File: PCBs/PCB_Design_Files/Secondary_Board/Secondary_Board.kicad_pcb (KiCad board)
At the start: 4 copper layers, 40.3 x 57.1 mm, 46 parts, among them IC1 TLV2333IDGKR, IC2 320S14-U, J1 Conn_FFC_8pin, J2 Conn_01x08_Pin, Q3 MMBT3904, Q4 MMBT3904, Q5 2N7002, Q6 BSS84, Q7 2N7002, Q8 BSS84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

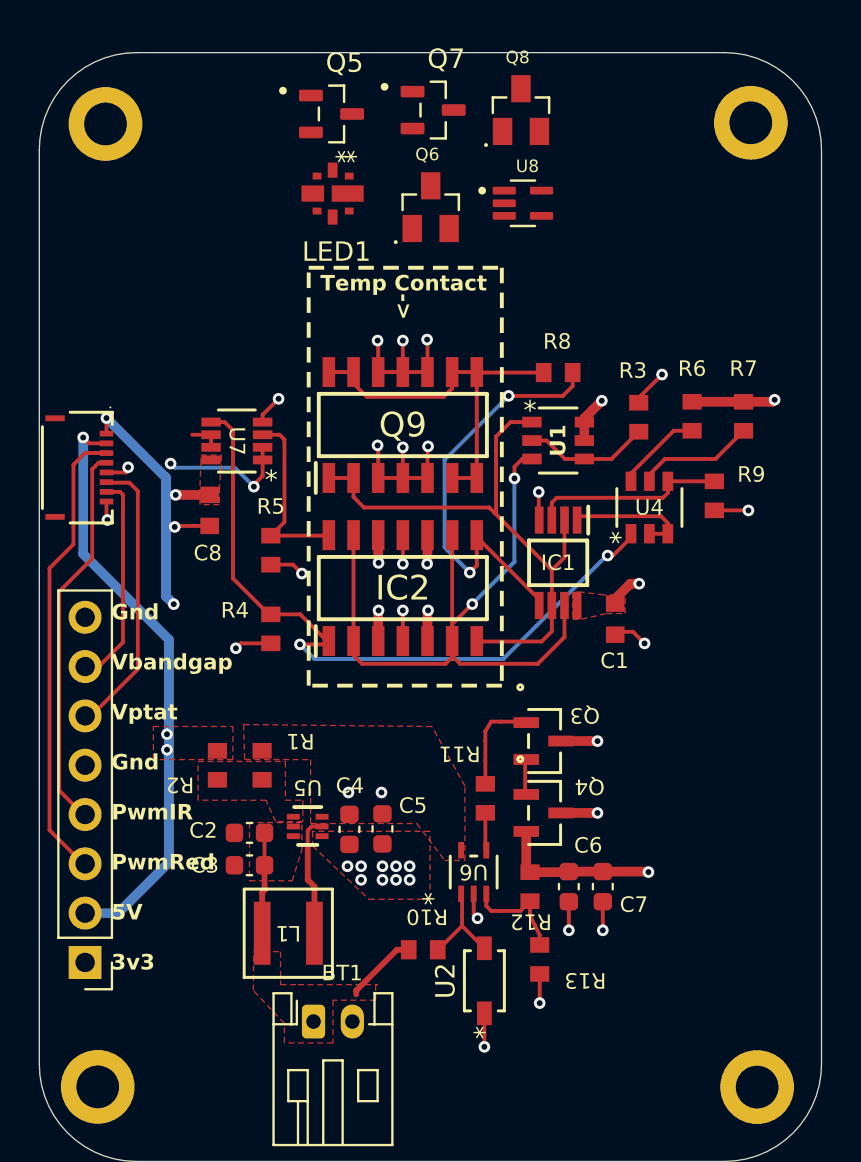
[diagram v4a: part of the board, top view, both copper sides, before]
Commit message: cleaned up ptat laout, 3v3 layer
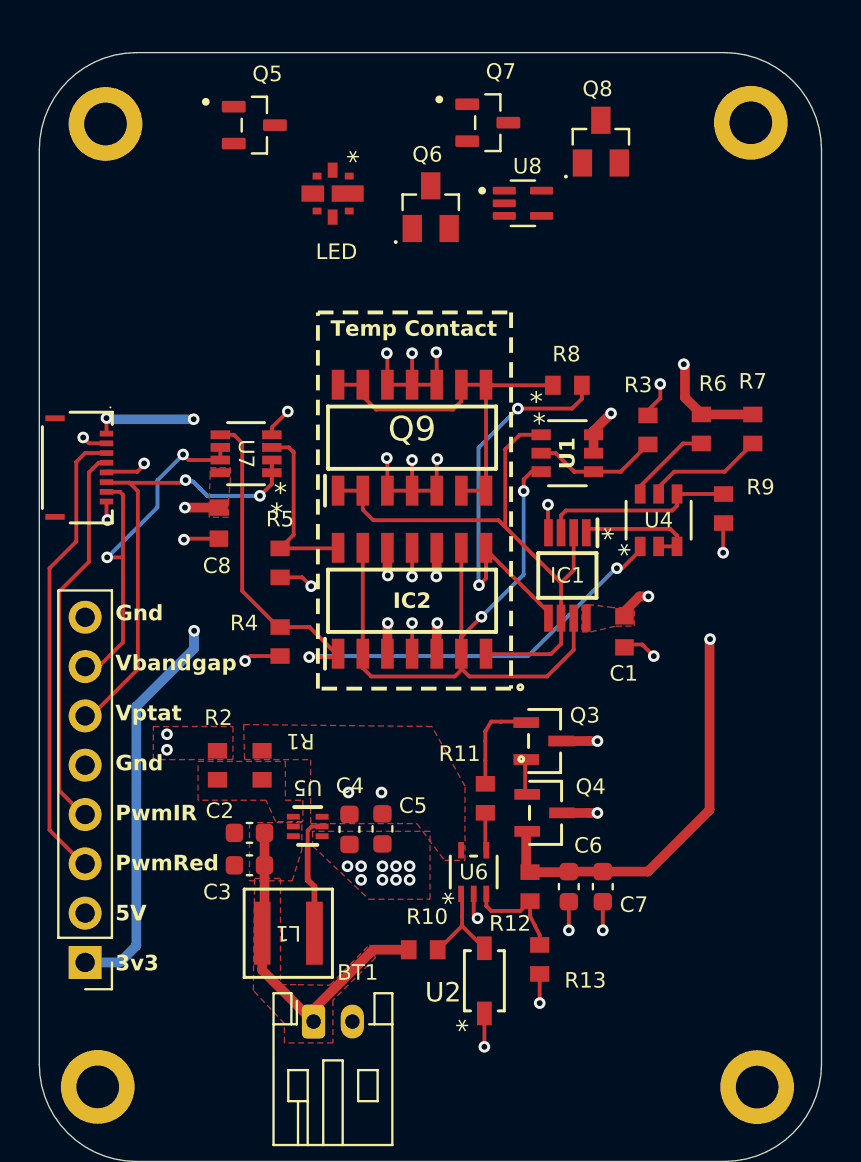
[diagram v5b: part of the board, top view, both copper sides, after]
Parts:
- IC1: value TLV2333IDGKR -> SOP65P490X110-8N
- J1: value Conn_FFC_8pin -> CON_5034800800_MOL
- Q5, Q7: value 2N7002 -> SOT95P240X111-3N
- Q6, Q8: value BSS84 -> SOT95P240X120-3N
- U7: value TLV9002 -> SOT_9002IDDFR_TEX
- moved Q8 4.42 mm to (136.5, 49.1)
- moved Q5 4.02 mm to (118.7, 48.2)
- moved Q7 2.89 mm to (130.7, 48.1)
- moved R3 0.81 mm to (138.9, 63.9)
- moved R6 0.81 mm to (141.7, 63.9)
- moved Q9 0.81 mm to (126.8, 64.3)
- moved C1 0.81 mm to (137.7, 74.3)
- moved IC1 0.81 mm to (134.8, 71.4)
- moved R4 0.81 mm to (120.0, 74.8)
- moved R5 0.81 mm to (120.0, 70.8)
- moved R7 0.81 mm to (144.3, 63.9)
- moved R9 0.81 mm to (142.8, 68.0)
- moved U1 0.81 mm to (134.8, 65.1)
- moved U4 0.81 mm to (139.5, 68.6)
- moved C8 0.81 mm to (116.8, 68.7)
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- renumbered LED1 to LED
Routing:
- net +5V: track 34.2 -> 5.08 mm
- net +3V3: track 36.3 -> 64.9 mm, vias 11 -> 12
- net +3.7V: track 9.07 -> 17.9 mm
- net /V_bandgap: track 13.3 -> 22.1 mm, vias 0 -> 2
- net /V_ptat: track 23.2 -> 25.5 mm
- net /PTAT_Bandgap/Pnp_In+: track 22.5 -> 21.4 mm
- net /PTAT_Bandgap/Vbg: track 37.0 -> 36.3 mm
- net GND: track 36.0 -> 36.5 mm
- added copper zone on In2.Cu, net +5V
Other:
- board text removed: "->"

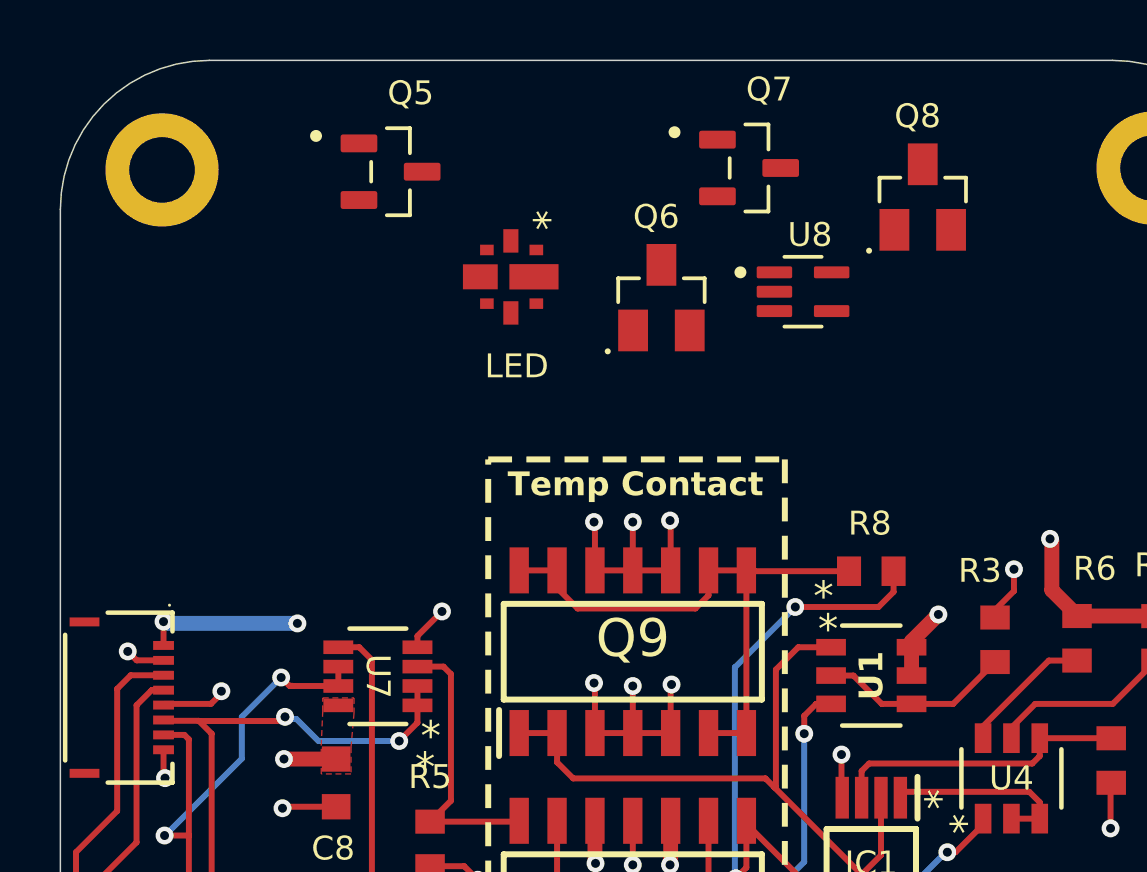
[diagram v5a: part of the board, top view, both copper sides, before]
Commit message: LED Driver added to PCB
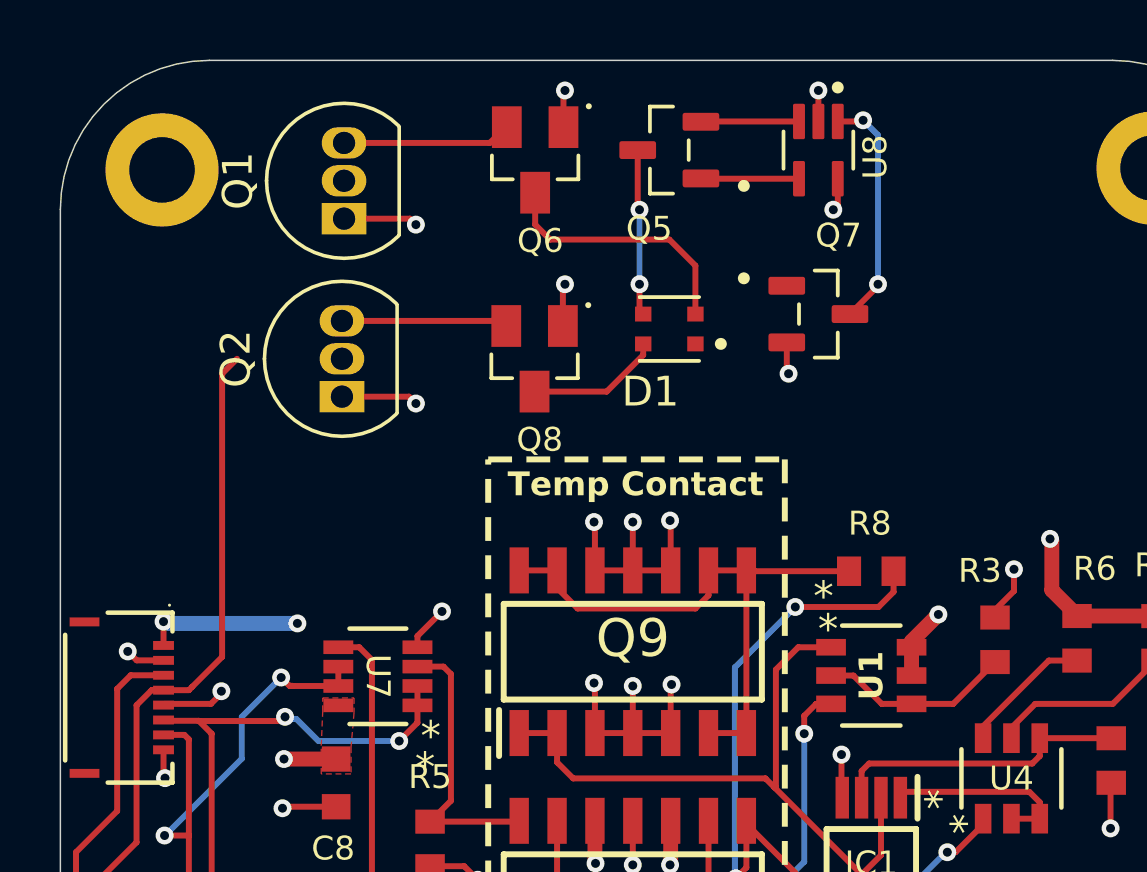
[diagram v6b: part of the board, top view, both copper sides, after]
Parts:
- removed LED: SFH 7018A, Project Footprints:SFH_7018A_LEDs
- added D1: VSMD66694, Project Footprints:DIO_VSMD66694, F.Cu at (128.0, 53.5)
- added Q1: 2N3904, Package_TO_SOT_THT:TO-92_Inline, F.Cu at (117.1, 49.8)
- added Q2: 2N3904, Package_TO_SOT_THT:TO-92_Inline, F.Cu at (117.0, 55.8)
- IC1: value SOP65P490X110-8N -> TLV2333IDGKR
- J1: value CON_5034800800_MOL -> Conn_FFC_8pin
- Q5, Q7: value SOT95P240X111-3N -> 2N7002
- Q6, Q8: value SOT95P240X120-3N -> BSS84
- U7: value SOT_9002IDDFR_TEX -> TLV9002
- moved Q8 14.1 mm to (123.5, 54.5), turned to 180 degrees
- moved Q5 9.38 mm to (128.0, 47.5), turned to 180 degrees
- moved Q6 6.27 mm to (123.5, 47.8), turned to 180 degrees
- moved Q7 5.42 mm to (133.0, 53.0)
- moved U8 4.78 mm to (133.0, 47.5), turned to -90 degrees
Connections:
- net /PWM_IR renamed /MCU_IR
- net /PWM_Red renamed /MCU_Red
- Q5 pad 1: unconnected-(Q5-Pad1) -> Net-(U8-OUT)
- Q5 pad 2: unconnected-(Q5-Pad2) -> Net-(U8--IN)
- Q5 pad 3: unconnected-(Q5-Pad3) -> /LED_Driver/Current Sink
- Q6 pad 1: unconnected-(Q6-G-Pad1) -> +5V
- Q6 pad 2: unconnected-(Q6-S-Pad2) -> Net-(Q1-C)
- Q6 pad 3: unconnected-(Q6-D-Pad3) -> Net-(Q6-D)
- Q7 pad 2: unconnected-(Q7-Pad2) -> GND
- Q7 pad 3: unconnected-(Q7-Pad3) -> /LED_Driver/Vbandgap
- Q8 pad 1: unconnected-(Q8-G-Pad1) -> +5V
- Q8 pad 2: unconnected-(Q8-S-Pad2) -> Net-(Q2-C)
- Q8 pad 3: unconnected-(Q8-D-Pad3) -> Net-(Q8-D)
- U8 pad 1: unconnected-(U8-+IN-Pad1) -> /LED_Driver/Vbandgap
- U8 pad 2: unconnected-(U8-V--Pad2) -> GND
- U8 pad 3: unconnected-(U8--IN-Pad3) -> Net-(U8--IN)
- U8 pad 4: unconnected-(U8-OUT-Pad4) -> Net-(U8-OUT)
- U8 pad 5: unconnected-(U8-V+-Pad5) -> +5V
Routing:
- net /MCU_IR: track 19.9 -> 32.5 mm
- net Net-(Q6-D): track 0.00 -> 8.64 mm
- net (no net): track 0.00 -> 7.96 mm
- net GND: track 36.5 -> 43.7 mm, vias 34 -> 38
- net Net-(Q1-C): track 0.00 -> 5.64 mm
- net Net-(Q2-C): track 0.00 -> 5.58 mm
- net /LED_Driver/Current Sink: track 0.00 -> 5.58 mm, vias 0 -> 2
- net Net-(Q8-D): track 0.00 -> 4.53 mm
- net +5V: track 5.08 -> 9.16 mm, vias 5 -> 8
- net Net-(U8-OUT): track 0.00 -> 3.29 mm
- net Net-(U8--IN): track 0.00 -> 3.29 mm
- net /LED_Driver/Vbandgap: vias 0 -> 2

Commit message: LED Driver Updates
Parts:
- added R14: 1k, Resistor_SMD:R_0603_1608Metric_Pad0.98x0.95mm_HandSolder, F.Cu at (110.8, 54.2)
- added R15: 10k, Resistor_SMD:R_0603_1608Metric_Pad0.98x0.95mm_HandSolder, F.Cu at (110.8, 52.7)
- added R16: R, Resistor_SMD:R_0603_1608Metric_Pad0.98x0.95mm_HandSolder, F.Cu at (110.8, 57.2)
- added R17: 10k, Resistor_SMD:R_0603_1608Metric_Pad0.98x0.95mm_HandSolder, F.Cu at (110.8, 55.7)
- added R18: 60, Resistor_SMD:R_0603_1608Metric_Pad0.98x0.95mm_HandSolder, F.Cu at (137.9, 49.0)
- added R19: 1k, Resistor_SMD:R_0603_1608Metric_Pad0.98x0.95mm_HandSolder, F.Cu at (137.9, 50.5)
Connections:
- net /LED_Driver/Vbandgap renamed Vbandgap
- net /MCU_IR renamed MCU_IR
- net /MCU_Red renamed MCU_Red
- Q7 pad 1: unconnected-(Q7-Pad1) -> Net-(Q7-Pad1)
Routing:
- net MCU_Red: track 23.7 -> 39.4 mm
- net Net-(Q1-B): track 0.00 -> 8.90 mm
- net Net-(Q1-C): track 5.64 -> 14.5 mm
- net Net-(U8--IN): track 3.29 -> 11.8 mm
- net Vbandgap: track 0.00 -> 7.96 mm
- net (no net): track 7.96 -> 0.00 mm
- net Net-(Q2-B): track 0.00 -> 6.43 mm
- net Net-(Q2-C): track 5.58 -> 11.9 mm
- net Net-(Q7-Pad1): track 0.00 -> 6.28 mm
- net +5V: track 9.16 -> 11.7 mm, vias 8 -> 10
- net GND: track 43.7 -> 44.7 mm, vias 38 -> 39
- net MCU_IR: track 32.5 -> 33.2 mm

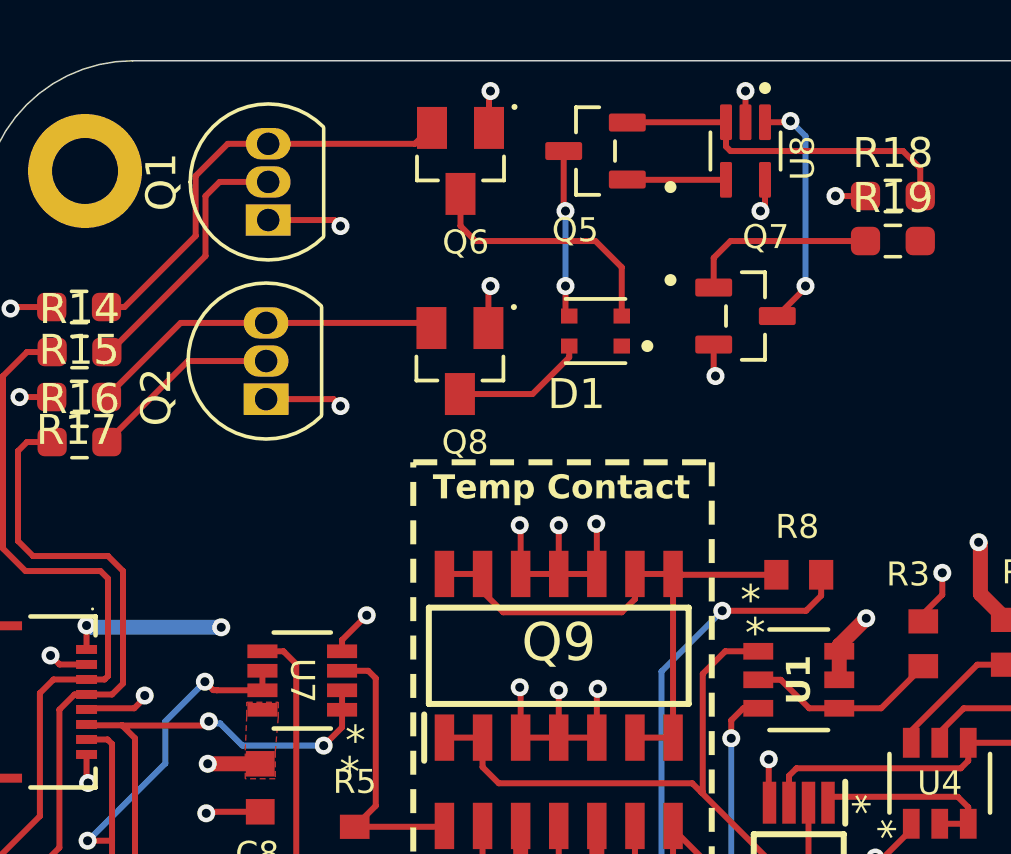
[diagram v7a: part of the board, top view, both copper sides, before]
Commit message: LED Driver updates
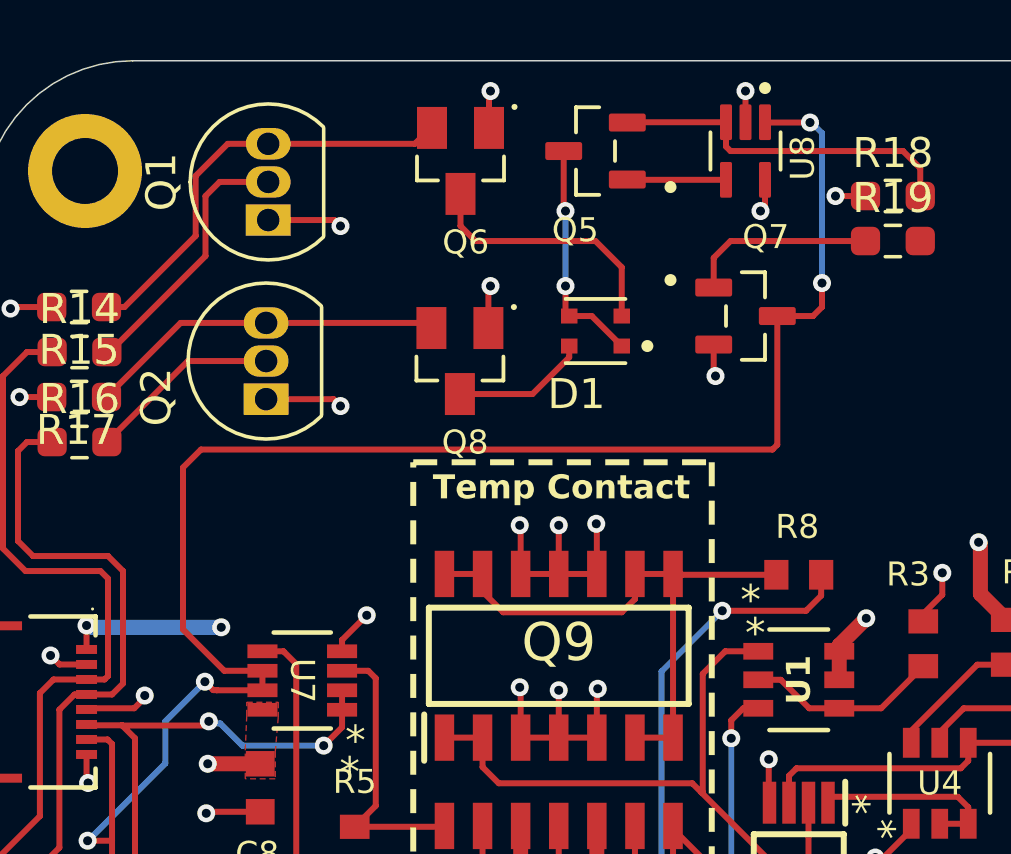
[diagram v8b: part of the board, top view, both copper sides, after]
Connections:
- J1 pad 7: /V_bandgap -> V_bandgap
- J2 pad 7: /V_bandgap -> V_bandgap
- Q7 pad 3: Vbandgap -> V_bandgap
- U7 pad 6: /V_bandgap -> V_bandgap
- U7 pad 7: /V_bandgap -> V_bandgap
- U8 pad 1: Vbandgap -> V_bandgap
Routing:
- net V_bandgap: track 0.00 -> 64.6 mm, vias 0 -> 4
- net /V_bandgap: track 22.1 -> 0.00 mm, vias 2 -> 0
- net Vbandgap: track 7.96 -> 0.00 mm, vias 2 -> 0
- net /LED_Driver/Current Sink: track 5.58 -> 7.74 mm
